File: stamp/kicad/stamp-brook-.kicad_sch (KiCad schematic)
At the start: 17 parts, among them J10 Conn_01x02_Female, J2 Conn_01x05_Male, J3 Screw_Terminal_01x20, J4 Conn_01x04_Female, J5 Conn_01x05_Male, J6 Conn_01x04_Female, J7 Conn_01x04_Male, J8 Conn_01x04_Male, J9 Conn_02x10_Odd_Even, U1 RP2040_Stamp

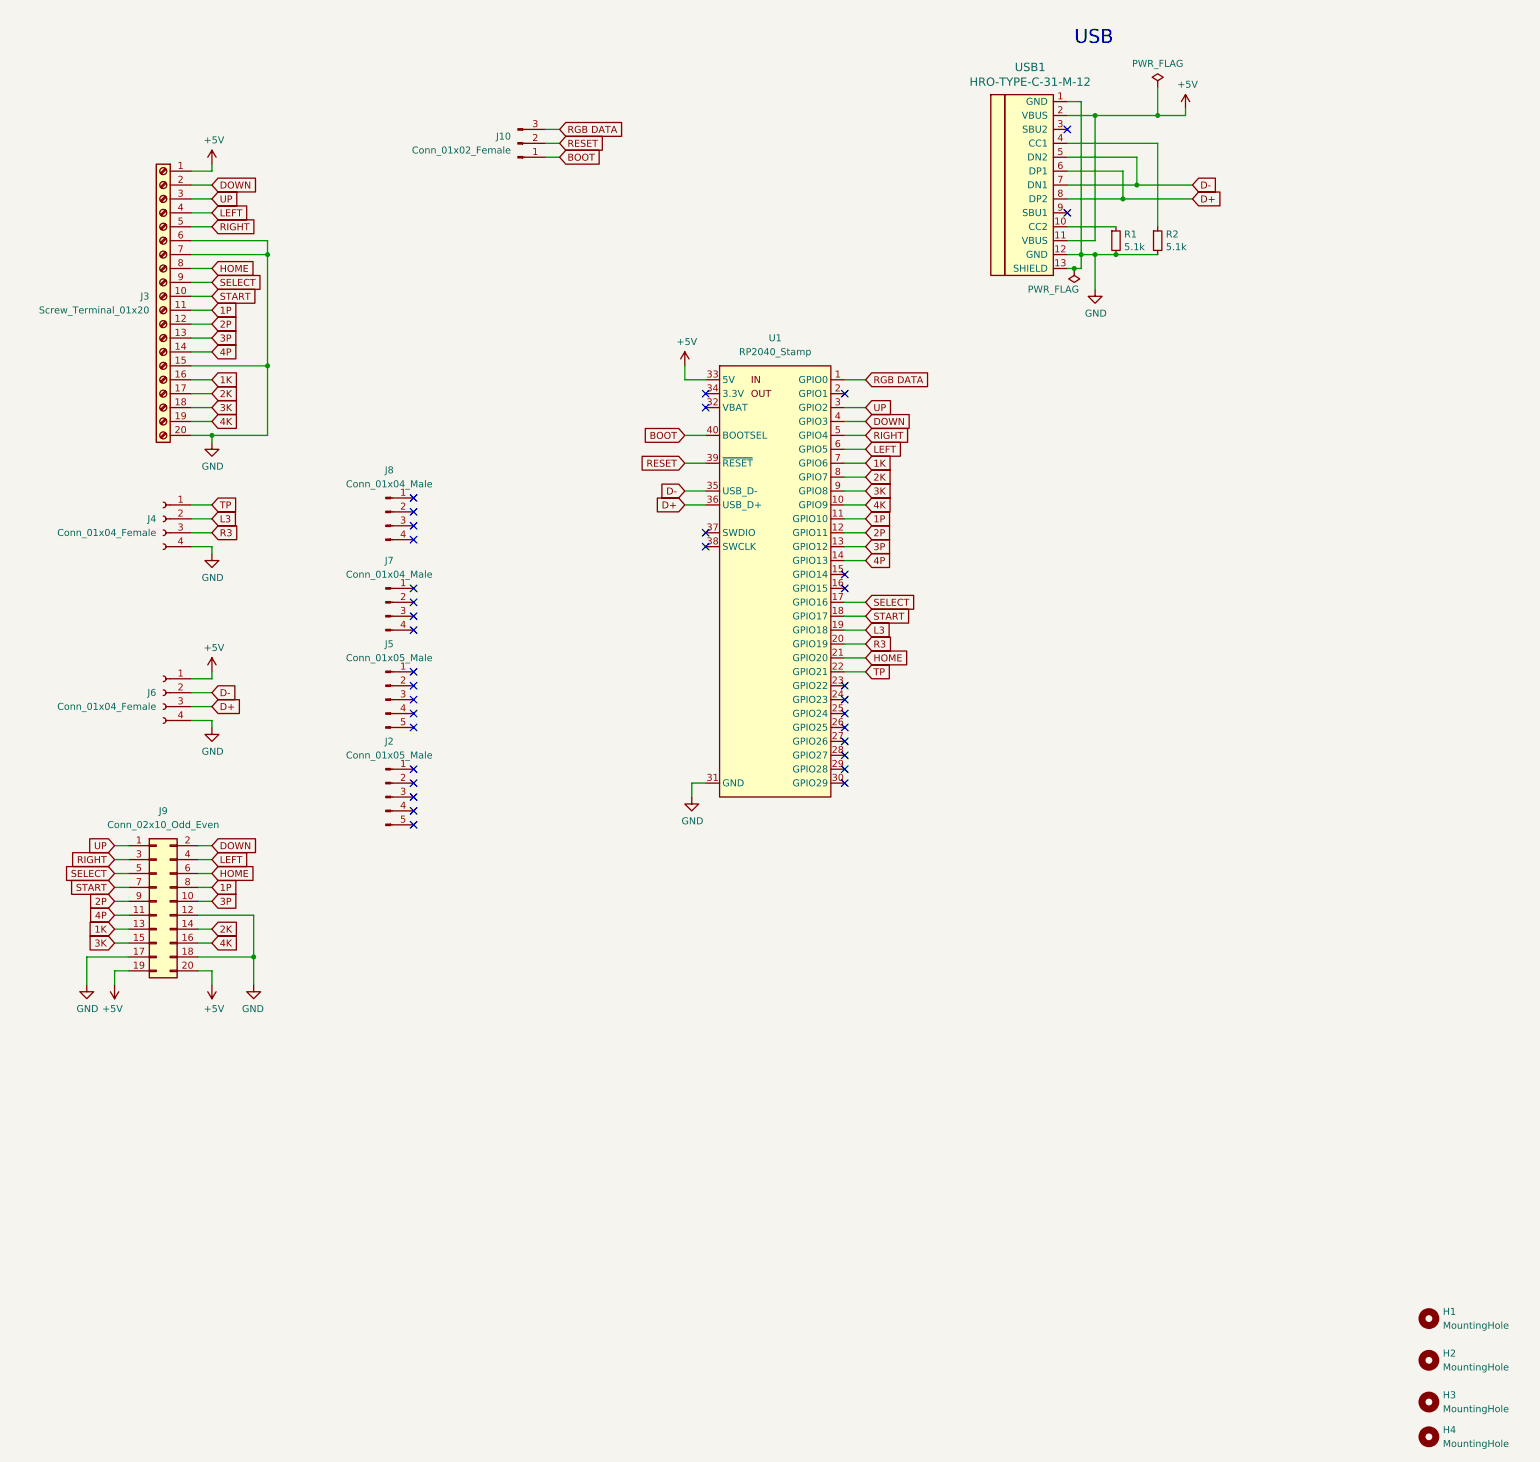
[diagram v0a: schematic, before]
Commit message: Add Turbo pins, OLED pins, and LS/DP/RS pins. Change Resistors to larger component
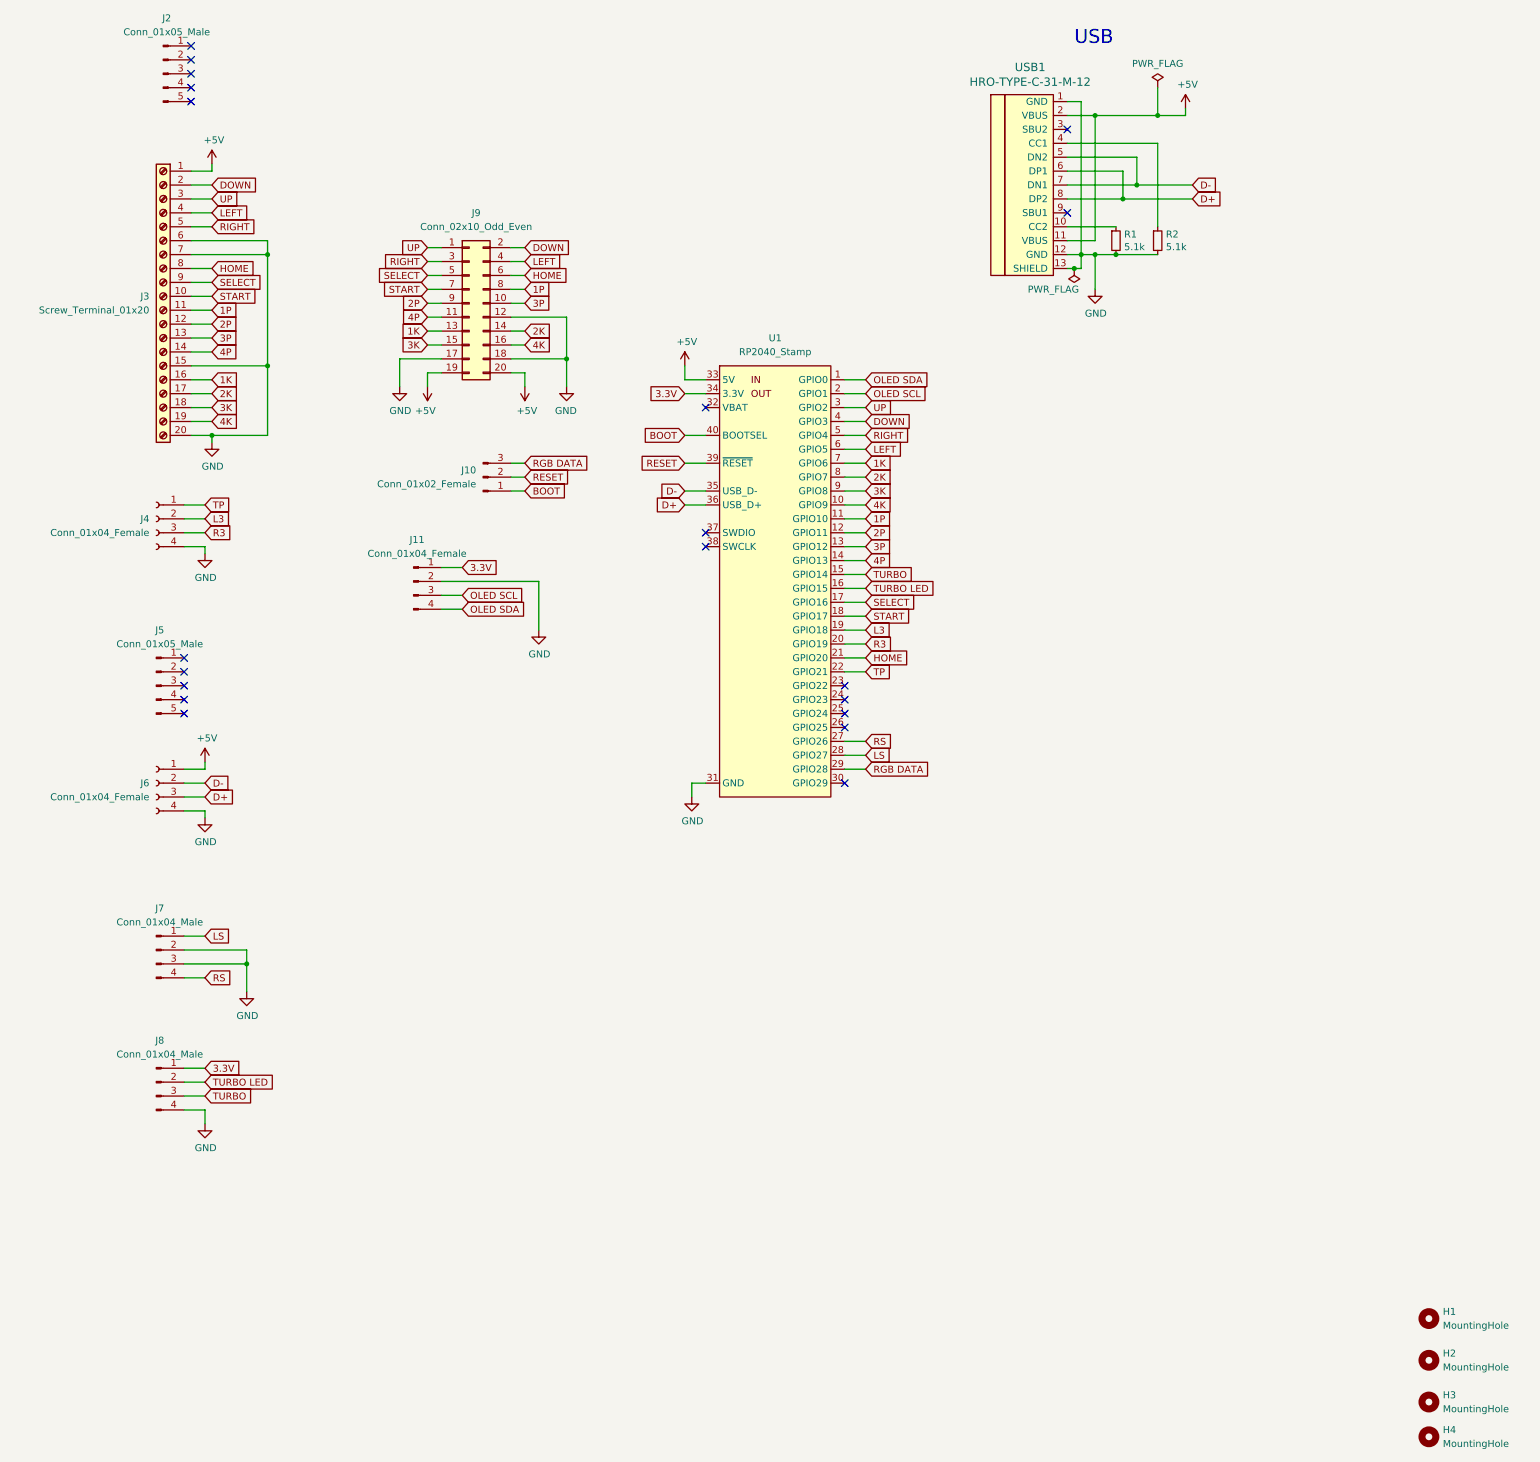
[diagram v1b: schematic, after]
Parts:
- added J11: Conn_01x04_Female, Connector_PinHeader_2.54mm:PinHeader_1x04_P2.54mm_Vertical, symbol Connector:Conn_01x04_Male
- R1, R2: footprint Resistor_SMD:R_0402_1005Metric -> CRCW25125K10JNTG:RESC6332X70N
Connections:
- net GND: now also J7.2 (Pin_2), J7.3 (Pin_3), J8.4 (Pin_4), J11.2 (Pin_2)
- net RGB DATA: now also U1.29 (GPIO28); no longer U1.1 (GPIO0)
- net TURBO: now reaches U1.15 (GPIO14)
- net TURBO: now also J8.3 (Pin_3)
- net TURBO LED: now reaches U1.16 (GPIO15)
- net TURBO LED: now also J8.2 (Pin_2)
- net OLED SCL: now reaches U1.2 (GPIO1)
- net OLED SCL: now also J11.3 (Pin_3)
- net RS: now reaches U1.27 (GPIO26)
- net RS: now also J7.4 (Pin_4)
- net LS: now reaches U1.28 (GPIO27)
- net LS: now also J7.1 (Pin_1)
- net 3.3V: now reaches U1.34 (3.3V)
- net 3.3V: now also J8.1 (Pin_1), J11.1 (Pin_1)
- new net OLED SDA: J11.4 (Pin_4), U1.1 (GPIO0)
- no-connect marks 35 -> 20
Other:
- moved on the sheet: J10, J2, J4, J5, J6, J7, J8, J9

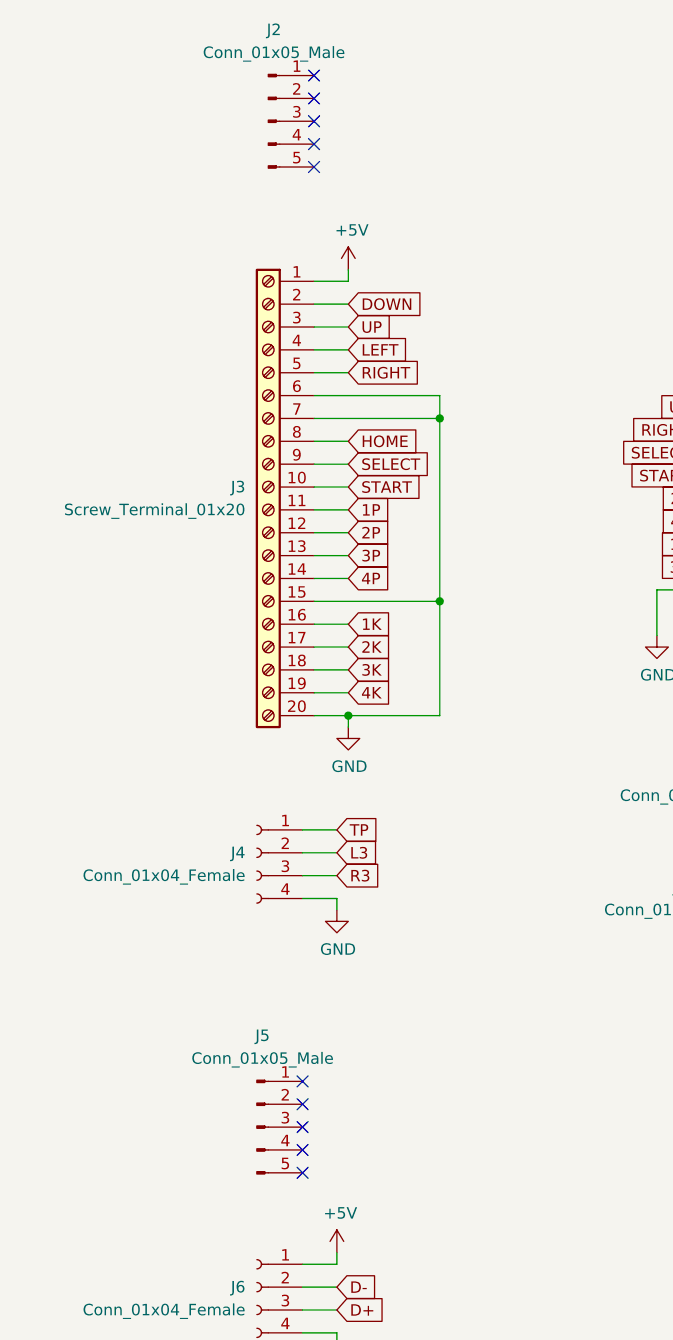
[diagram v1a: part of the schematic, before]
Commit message: Minor adjustments to traces, remove J2 and J5 due to nonuse
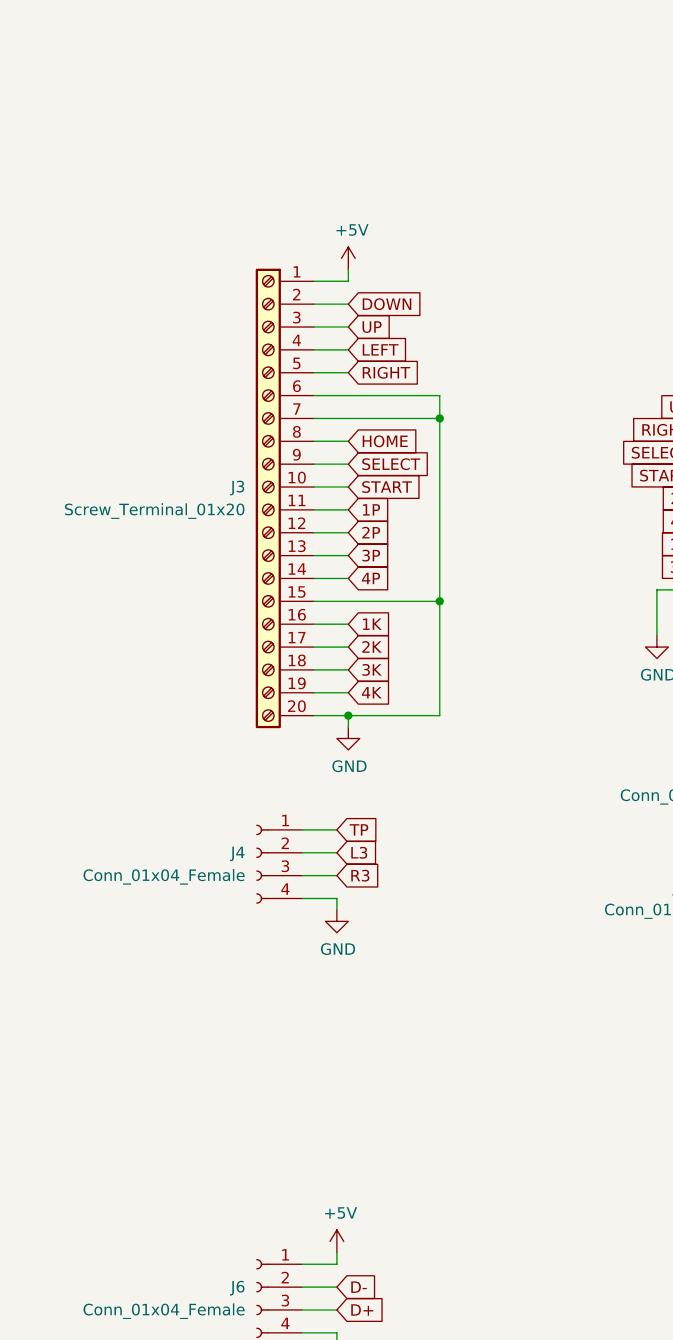
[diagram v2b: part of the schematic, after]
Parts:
- removed J2, J5: Conn_01x05_Male, Connector_PinHeader_2.00mm:PinHeader_1x05_P2.00mm_Vertical, symbol Connector:Conn_01x05_Male
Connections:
- no-connect marks 20 -> 10
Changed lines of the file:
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@@
   (no_connect (at 171.45 146.05))
   (no_connect (at 171.45 143.51))
-  (no_connect (at 50.8 143.51))
-  (no_connect (at 50.8 135.89))
-  (no_connect (at 50.8 138.43))
-  (no_connect (at 50.8 140.97))
-  (no_connect (at 52.07 34.29))
-  (no_connect (at 50.8 146.05))
-  (no_connect (at 52.07 24.13))
-  (no_connect (at 52.07 26.67))
-  (no_connect (at 52.07 29.21))
-  (no_connect (at 52.07 31.75))
   (no_connect (at 212.09 39.37))
   (wire (pts (xy 212.09 62.23) (xy 214.63 62.23))
@@
     (pin "9")
   )
-  (symbol (lib_id "Connector:Conn_01x05_Male") (at 45.72 140.97 0) (unit 1)
-    (in_bom yes) (on_board yes) (fields_autoplaced)
-    (property "Reference" "J5" (id 0) (at 46.355 130.81 0))
-    (property "Value" "Conn_01x05_Male" (id 1) (at 46.355 133.35 0))
-    (property "Footprint" "Connector_PinHeader_2.00mm:PinHeader_1x05_P2.00mm_Vertical" (id 2) (at 45.72 140.97 0)
-      (effects (font (size 1.27 1.27)) hide)
-    )
-    (property "Datasheet" "~" (id 3) (at 45.72 140.97 0)
-      (effects (font (size 1.27 1.27)) hide)
-    )
-    (pin "1")
-    (pin "2")
-    (pin "3")
-    (pin "4")
-    (pin "5")
-  )
   (symbol (lib_id "power:GND") (at 120.65 86.36 0) (mirror y) (unit 1)
     (in_bom yes) (on_board yes)
@@
     (pin "4")
   )
-  (symbol (lib_id "Connector:Conn_01x05_Male") (at 46.99 29.21 0) (unit 1)
-    (in_bom yes) (on_board yes) (fields_autoplaced)
-    (property "Reference" "J2" (id 0) (at 47.625 19.05 0))
-    (property "Value" "Conn_01x05_Male" (id 1) (at 47.625 21.59 0))
-    (property "Footprint" "Connector_PinHeader_2.00mm:PinHeader_1x05_P2.00mm_Vertical" (id 2) (at 46.99 29.21 0)
-      (effects (font (size 1.27 1.27)) hide)
-    )
-    (property "Datasheet" "~" (id 3) (at 46.99 29.21 0)
-      (effects (font (size 1.27 1.27)) hide)
-    )
-    (pin "1")
-    (pin "2")
-    (pin "3")
-    (pin "4")
-    (pin "5")
-  )
   (symbol (lib_id "power:+5V") (at 54.61 154.94 0) (unit 1)
     (in_bom yes) (on_board yes)
@@
       (reference "H4") (unit 1) (value "MountingHole") (footprint "MountingHole:MountingHole_3.2mm_M3")
     )
-    (path "/a6d50896-f15e-45b0-81f6-d53b078764b2"
-      (reference "J2") (unit 1) (value "Conn_01x05_Male") (footprint "Connector_PinHeader_2.00mm:PinHeader_1x05_P2.00mm_Vertical")
-    )
     (path "/d18c544f-661a-495a-9d4f-ca9214eda290"
       (reference "J3") (unit 1) (value "Screw_Terminal_01x20") (footprint "Connector_Wago:Wago_734-150_1x20_P3.50mm_Vertical")
@@
       (reference "J4") (unit 1) (value "Conn_01x04_Female") (footprint "Connector_PinSocket_2.00mm:PinSocket_1x04_P2.00mm_Vertical")
     )
-    (path "/51e77ea7-ff52-4a5d-ada1-d961b6ef7642"
-      (reference "J5") (unit 1) (value "Conn_01x05_Male") (footprint "Connector_PinHeader_2.00mm:PinHeader_1x05_P2.00mm_Vertical")
-    )
     (path "/a220aa7e-8cad-45f5-a4bc-72eb7d34202c"
